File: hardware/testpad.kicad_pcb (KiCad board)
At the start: 4 copper layers, 58.2 x 93.2 mm, 69 parts, among them J1 HC-TYPE-C-16P-CB1.6, J3 AFA01-S08FCA-00, SW1 SSSS811101, SW2 SC4823S6-TR, SW3 SC4823S6-TR, SW4 SC4823S6-TR, SW5 SC4823S6-TR, T1 XL4067TS, U1 ESP32-C6-WROOM-1-N8, U2 BQ24074RGTR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

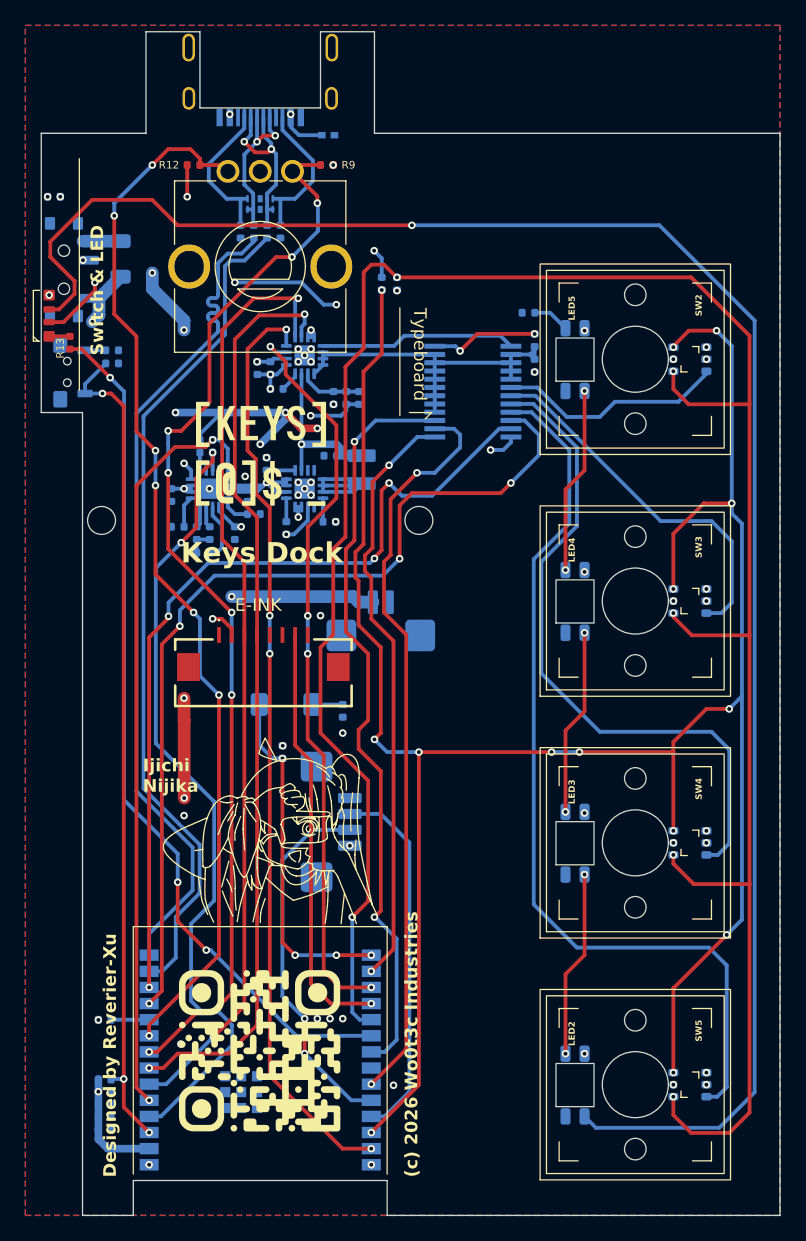
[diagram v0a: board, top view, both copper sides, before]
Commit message: :zap: improve led power supply
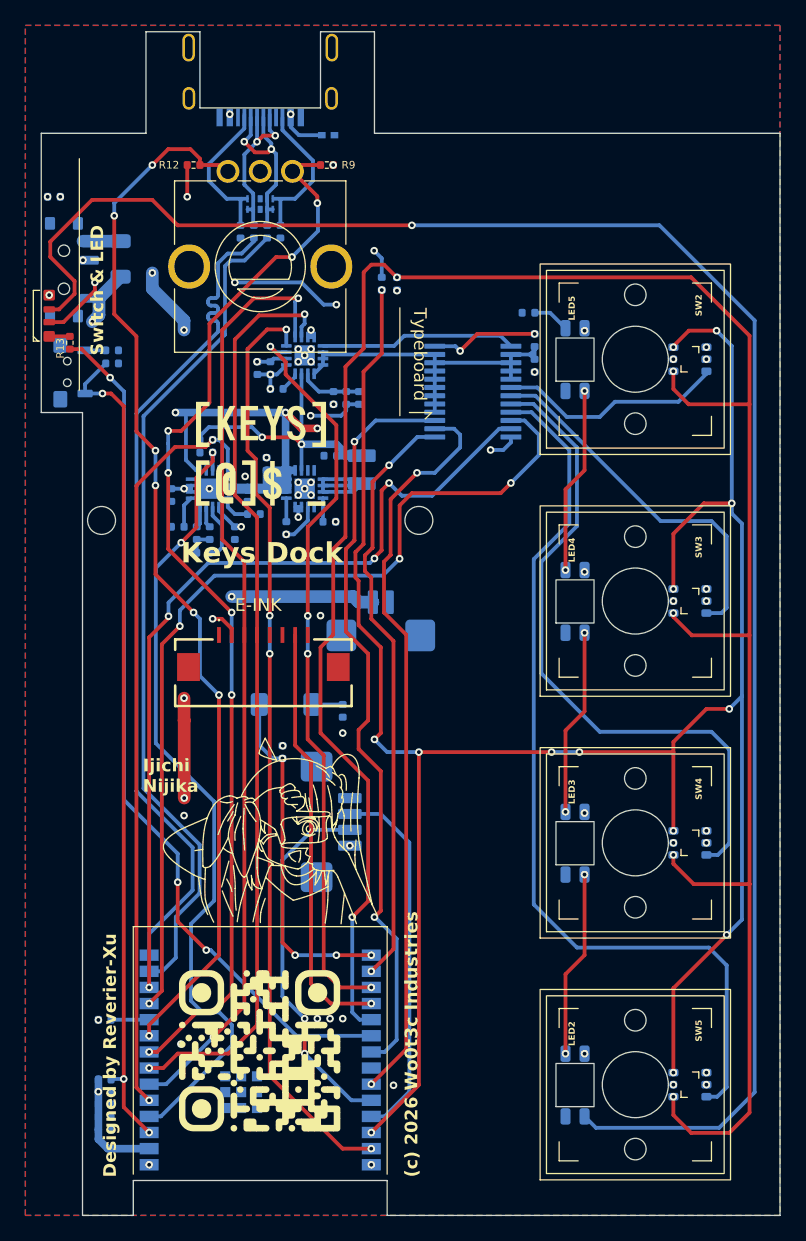
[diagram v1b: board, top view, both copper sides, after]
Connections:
- R17 pad 1: P,+5 -> P,+3.3
- R25 pad 1: P,+5 -> P,+3.3
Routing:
- net P,+3.3: track 282.4 -> 292.5 mm, vias 16 -> 17
- net P,+5: track 153.5 -> 146.1 mm, vias 10 -> 8
- net P,E: track 4.85 -> 3.37 mm, vias 29 -> 28
